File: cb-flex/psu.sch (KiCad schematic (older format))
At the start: 32 parts

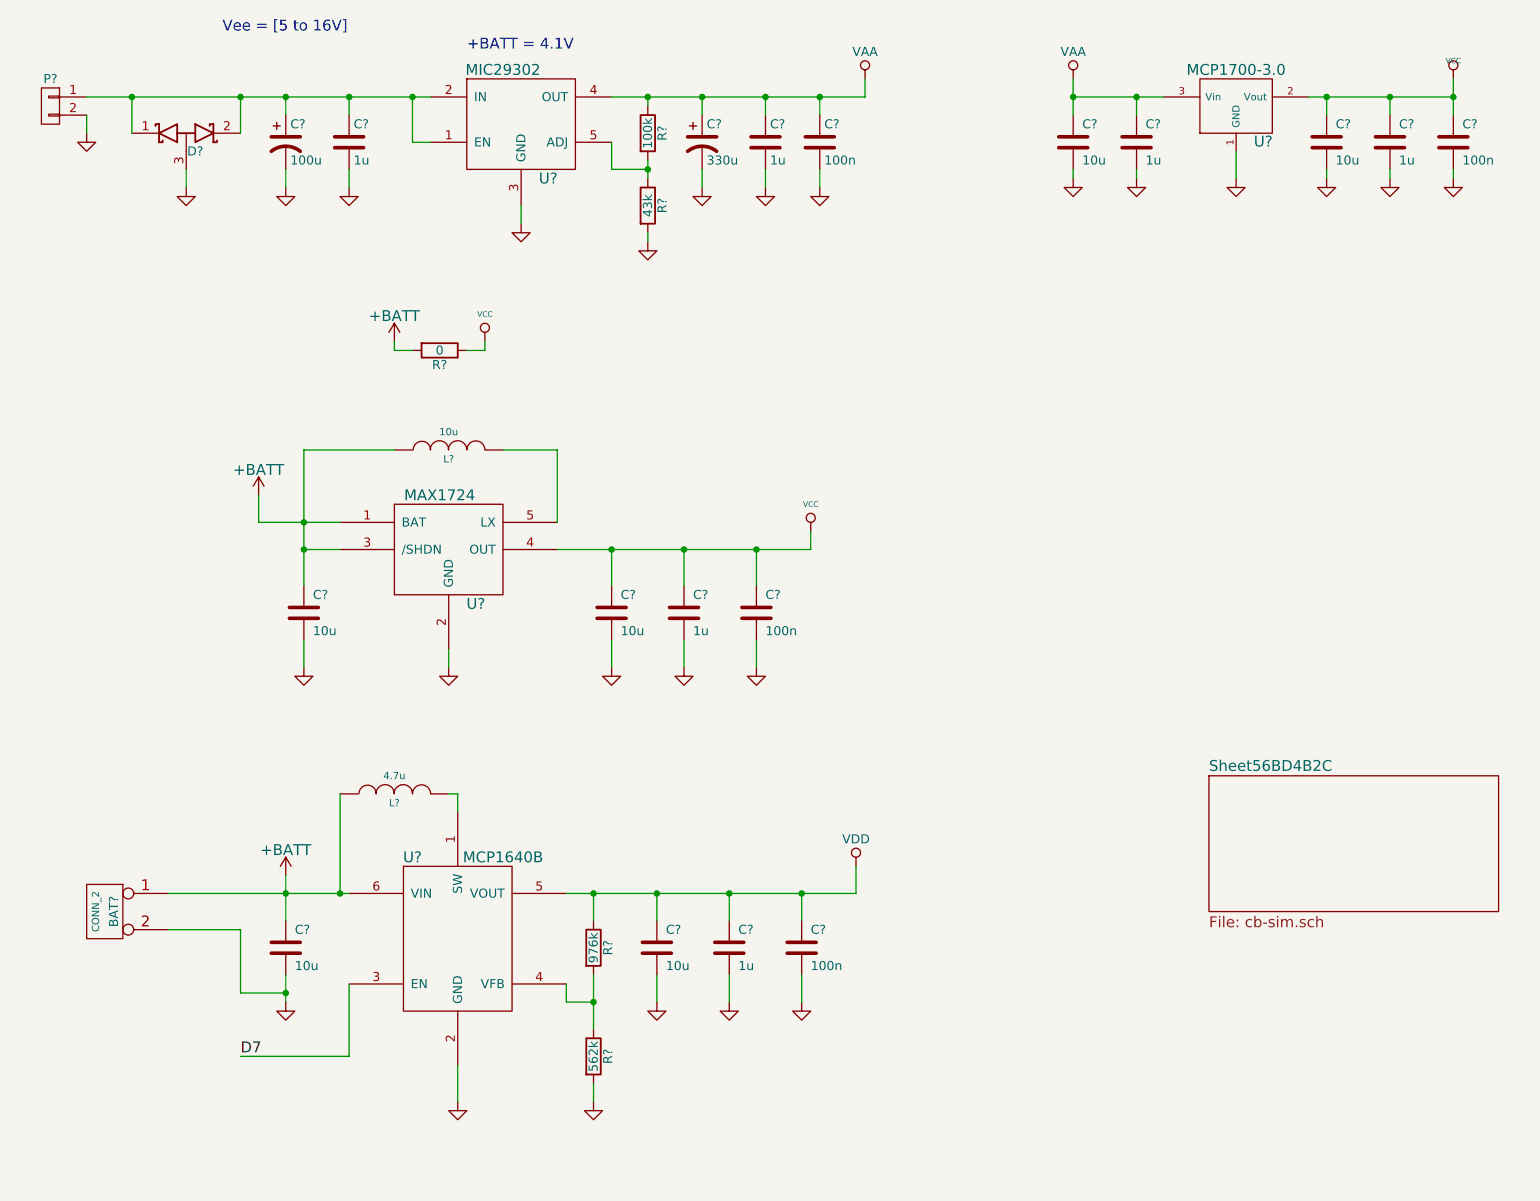
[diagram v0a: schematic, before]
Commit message: Finishing schematic and starting PCB layout
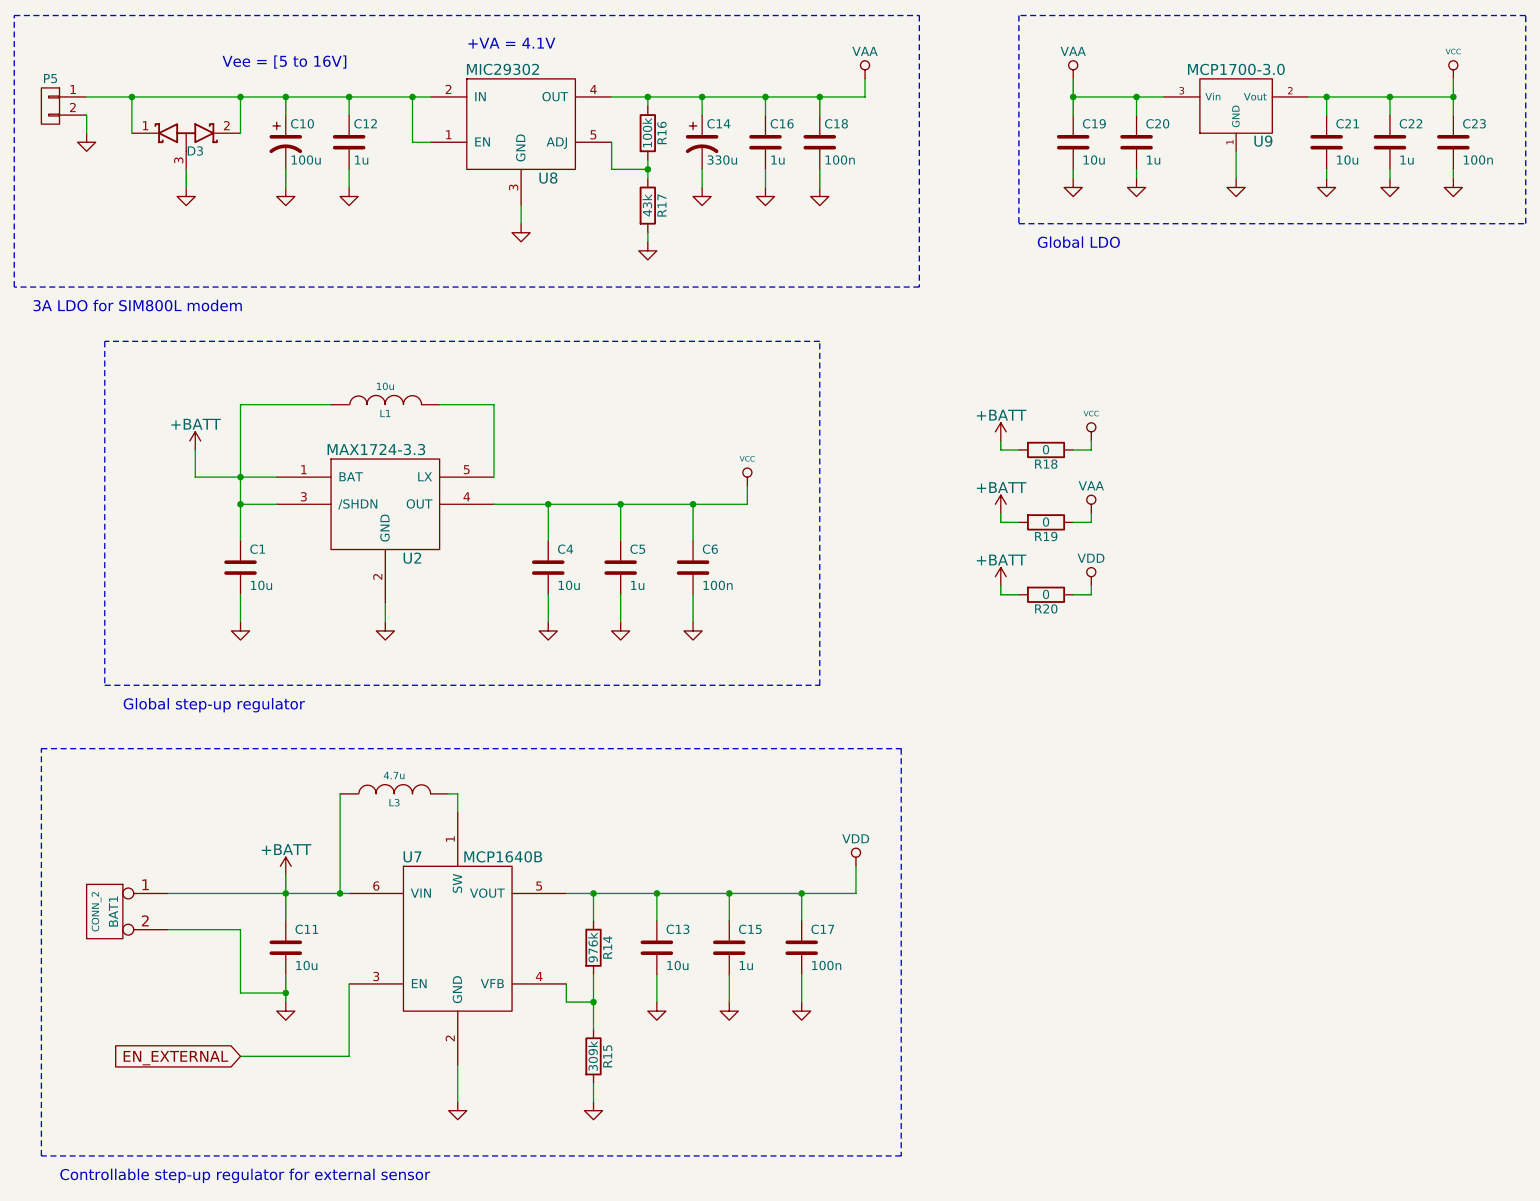
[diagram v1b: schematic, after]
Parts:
- added R18, R20: 0, mysmd:SM0603S, symbol R
- L3: renamed from L?; footprint Resistors_SMD:R_0805 -> libcms:SM0805
- R15: renamed from R?; value 562k -> 309k
- U2: renamed from U?; value MAX1724 -> MAX1724-3.3
- U7: renamed from U?; footprint Housings_SOT-23_SOT-143_TSOT-6:SOT-23-6 -> libcms:SOT23_6
- gave numbers to parts that had none: 28
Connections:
- net +BATT: now also R18.2, R20.2
- net VAA: now also R19.1
- net VCC: now also R18.1; no longer R19.1
- net VDD: now also R20.1
- net D7 renamed EN_EXTERNAL
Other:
- note added: "+VA = 4.1V"
- note added: "3A LDO for SIM800L modem"
- note added: "Controllable step-up regulator for external sensor"
- note added: "Global LDO"
- note added: "Global step-up regulator"
- note removed: "+BATT = 4.1V"
- moved on the sheet: C1, C4, C5, C6, L1, R19, U2

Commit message: Finishing layout
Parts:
- removed C23: 100n, old_mysmd:SM0603S, symbol C
- removed U9: MCP1700-3.0, libcms:SOT23, symbol MCP1702
- added U9: AP7365-30, libcms:SOT23-5, symbol AP7365
- C19: footprint old_mysmd:SM0603S -> mysmd:SM0603S
- C21: value 10u -> 1u
- C22: value 1u -> 100n
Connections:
- net GND: now also U9.2 (GND)
- net VAA: now also U9.1 (IN), U9.3 (EN)
- net VCC: now also U9.5 (OUT)
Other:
- moved on the sheet: R18, R19, R20
